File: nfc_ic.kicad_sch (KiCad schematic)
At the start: 7 parts, among them U3 NT3H2X11

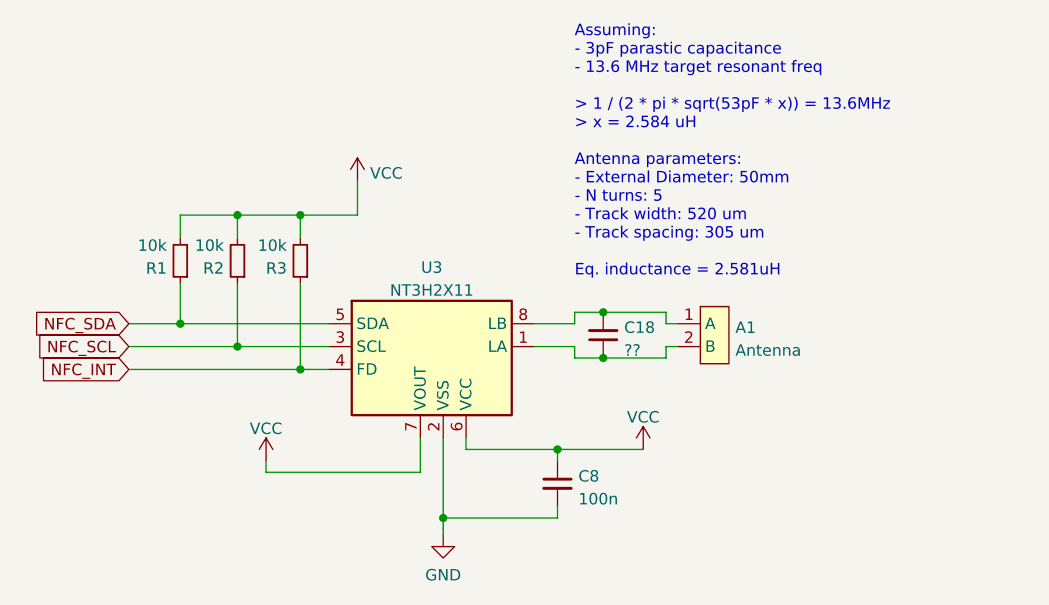
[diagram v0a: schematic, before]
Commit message: Add board REV-D
Revision D changes the mounting holes so that we can fit screws to
assemble the two case pieces.

Also add required compliance logos on the back.
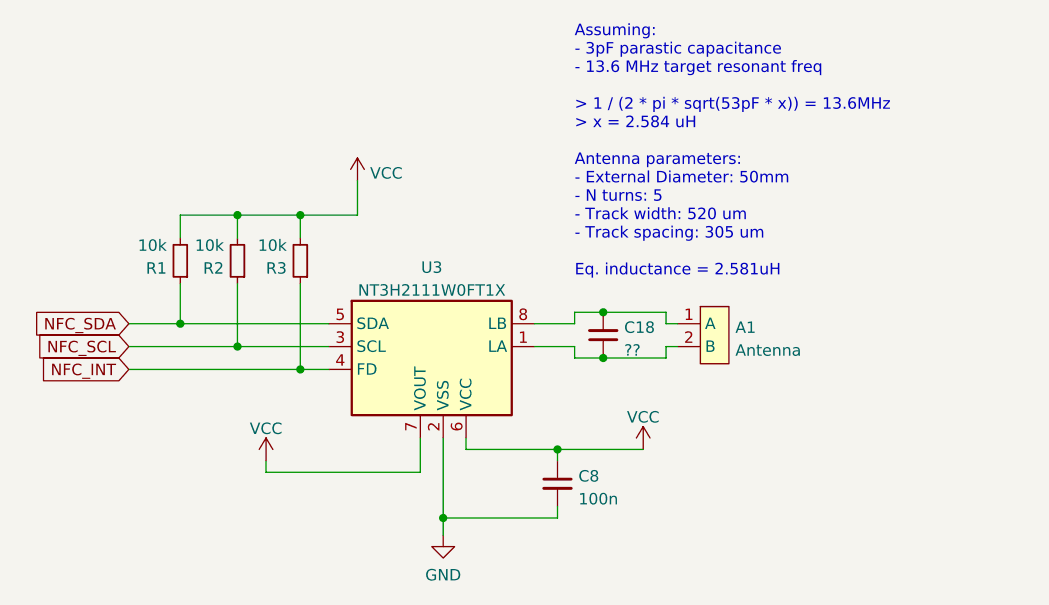
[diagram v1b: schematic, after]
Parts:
- U3: value NT3H2X11 -> NT3H2111W0FT1X
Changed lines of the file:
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@@
       (effects (font (size 1.27 1.27)))
     )
-    (property "Value" "NT3H2X11" (at 144.78 80.7521 0)
+    (property "Value" "NT3H2111W0FT1X" (at 144.78 80.7521 0)
       (effects (font (size 1.27 1.27)))
     )
